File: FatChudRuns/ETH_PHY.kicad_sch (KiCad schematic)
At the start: 58 parts, among them J1 RJ45_Pulse_JXD6-0001NL, U2 DP83848I

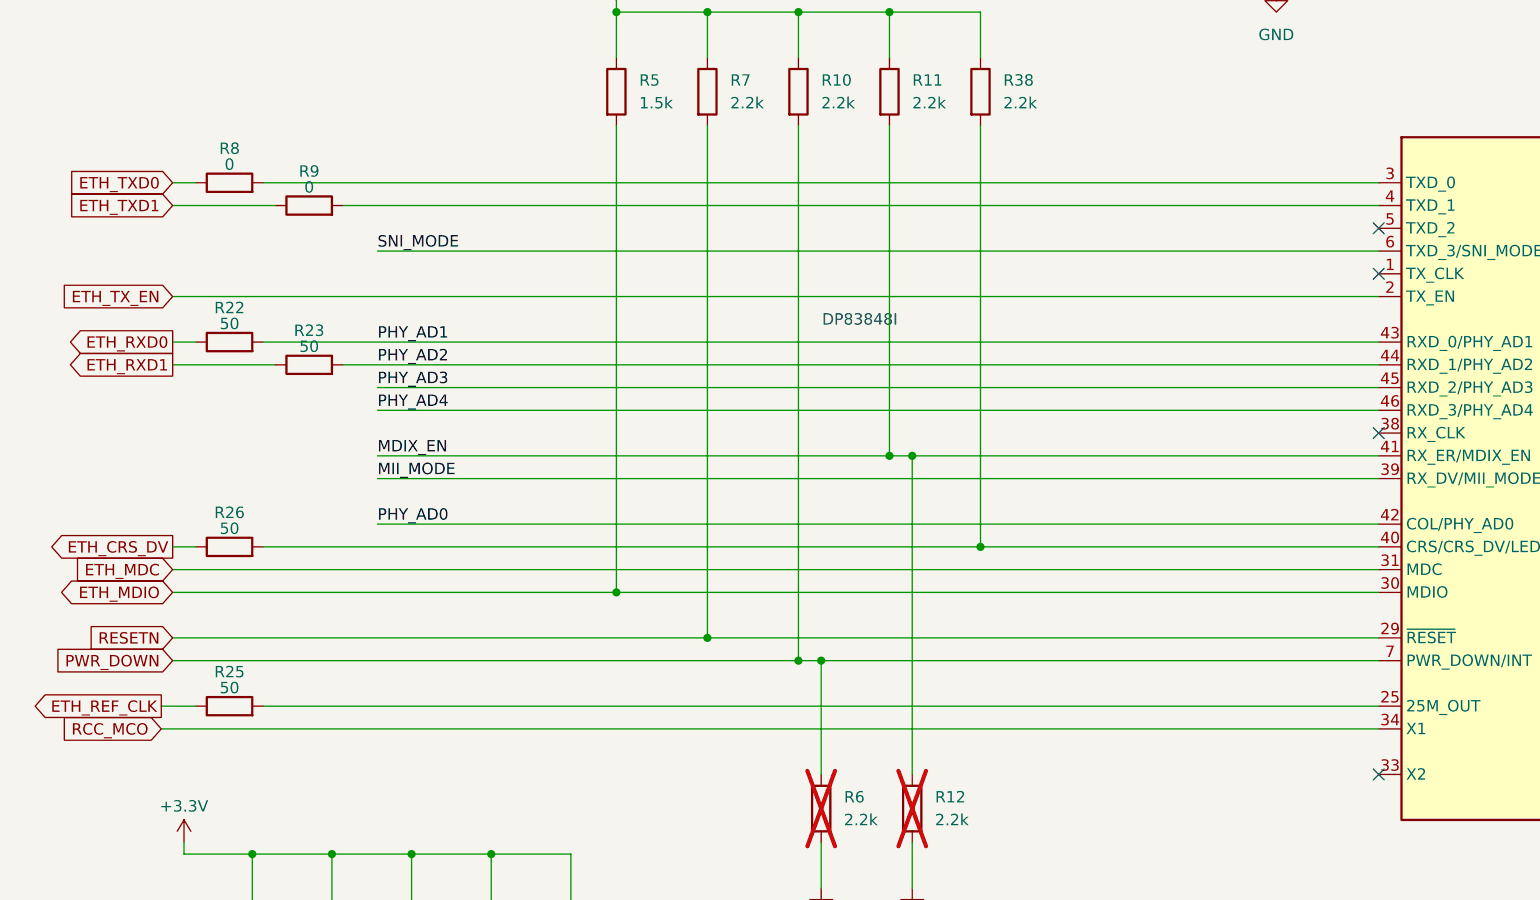
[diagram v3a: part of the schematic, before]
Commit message: routed phy usb and clock
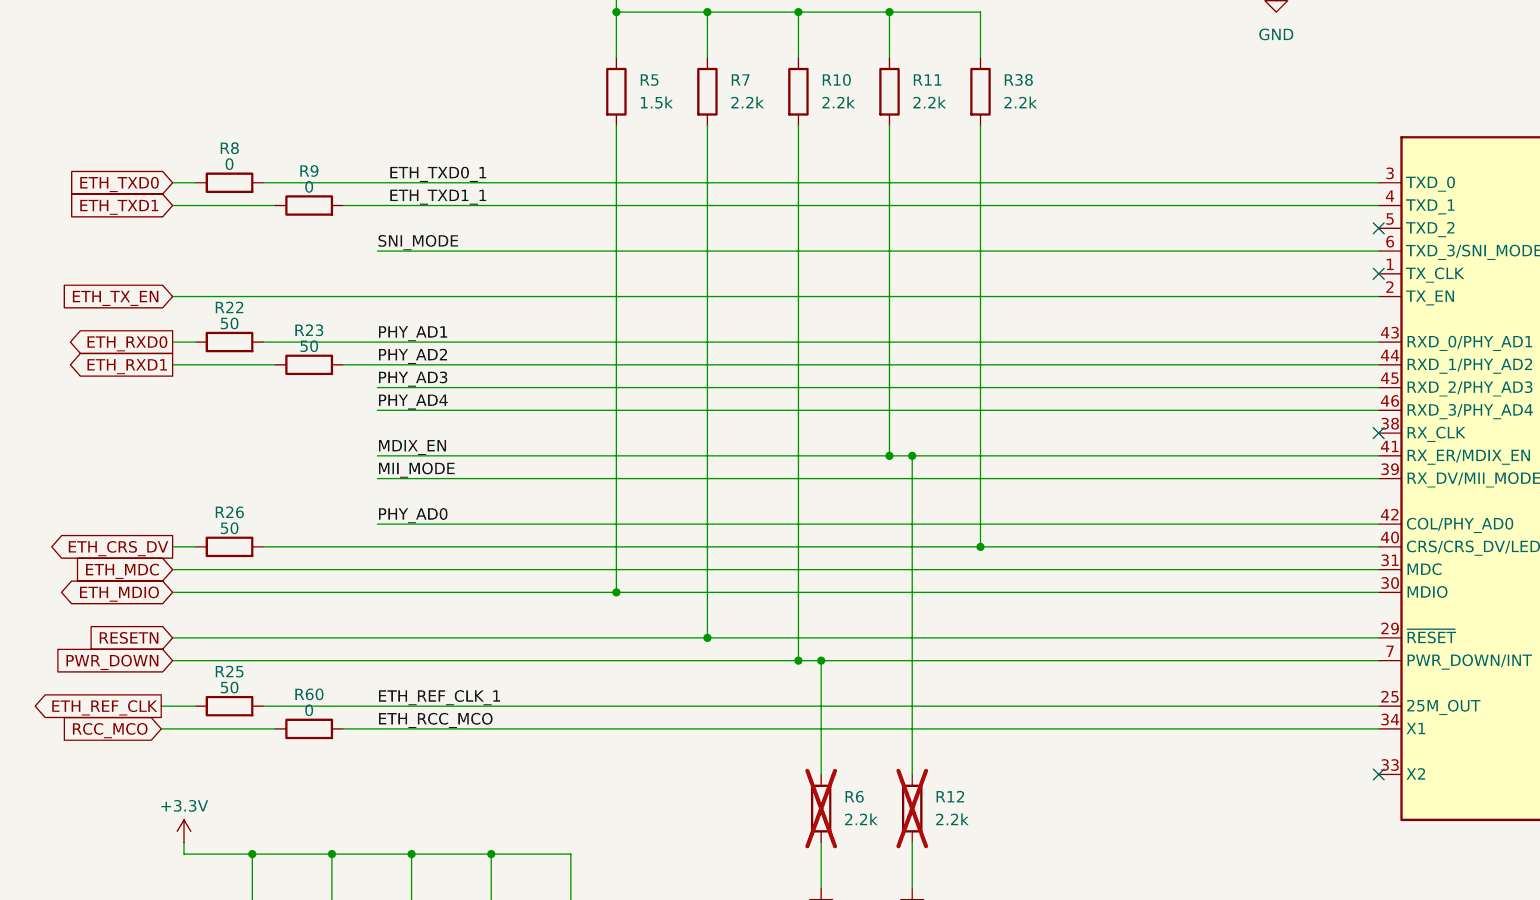
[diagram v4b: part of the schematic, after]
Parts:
- added R60: 0, Resistor_SMD:R_0603_1608Metric, symbol Device:R
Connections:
- net RCC_MCO: now also R60.1; no longer U2.34 (X1)
- net ETH_TXD1_1: now reaches R9.2, U2.4 (TXD_1)
- net ETH_REF_CLK_1: now reaches R25.2, U2.25 (25M_OUT)
- net ETH_TXD0_1: now reaches R8.2, U2.3 (TXD_0)
- new net ETH_RCC_MCO: R60.2, U2.34 (X1)
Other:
- note removed: "DP83848I"

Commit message: updated 3d model footprint for Rj45 (created new library)
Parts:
- J1: footprint Connector_RJ:RJ45_Pulse_JXD6-0001NL_Horizontal -> JXD6-0001NL:RJ45_Pulse_JXD6-0001NL_Horizontal
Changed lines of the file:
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@@
 			)
 		)
-		(property "Footprint" "Connector_RJ:RJ45_Pulse_JXD6-0001NL_Horizontal"
+		(property "Footprint" "JXD6-0001NL:RJ45_Pulse_JXD6-0001NL_Horizontal"
 			(at 355.6 73.66 0)
 			(hide yes)

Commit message: updated 10uF to 0805, completed BOM, sent to fab
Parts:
- C10, C12, C13, C14, C15, C16, C17, C18, C20, C28: JLCPCB Part # (none) -> C2181816; Manufacturer Number (none) -> C0603C104K4RAC
- C11, C19, C9: footprint Capacitor_SMD:C_0603_1608Metric -> Capacitor_SMD:C_0805_2012Metric; JLCPCB Part # (none) -> C2167271; Manufacturer Number (none) -> C0805C106K4PAC
- J1: JLCPCB Part # (none) -> C5359047; Manufacturer Number (none) -> JXD6-0001NL
- R10, R11, R14, R15, R18, R20, R24, R27, R30, R36, R37, R38, R41, R42, R43, R7: JLCPCB Part # (none) -> C113303; Manufacturer Number (none) -> RC0603JR-072K2L
- R22, R23, R25, R26, R31, R32, R33, R34: JLCPCB Part # (none) -> C849792; Manufacturer Number (none) -> RT0603BRE0750RL
- R35: JLCPCB Part # (none) -> C137709; Manufacturer Number (none) -> RC0603FR-074K87L
- R39, R40: JLCPCB Part # (none) -> C107696; Manufacturer Number (none) -> RC0603FR-07220RL
- R45, R46, R58, R59, R60, R8, R9: JLCPCB Part # (none) -> C95177; Manufacturer Number (none) -> RC0603JR-070RL
- R5: JLCPCB Part # (none) -> C114668; Manufacturer Number (none) -> RC0603FR-071K5L
- U2: JLCPCB Part # (none) -> C12082; Manufacturer Number (none) -> DP83848IVVX/NOPB
